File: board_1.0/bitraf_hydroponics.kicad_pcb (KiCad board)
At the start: 2 copper layers, 100 x 50 mm, 44 parts, among them P1 12V, P10 I2C_4, P11 BUZZ, P12 LDR, P13 TEMP_HUM, P14 PROGRAMMER, P15 SPI, P16 RADIO_433, P2 SWITCH_1, P3 SWITCH_2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

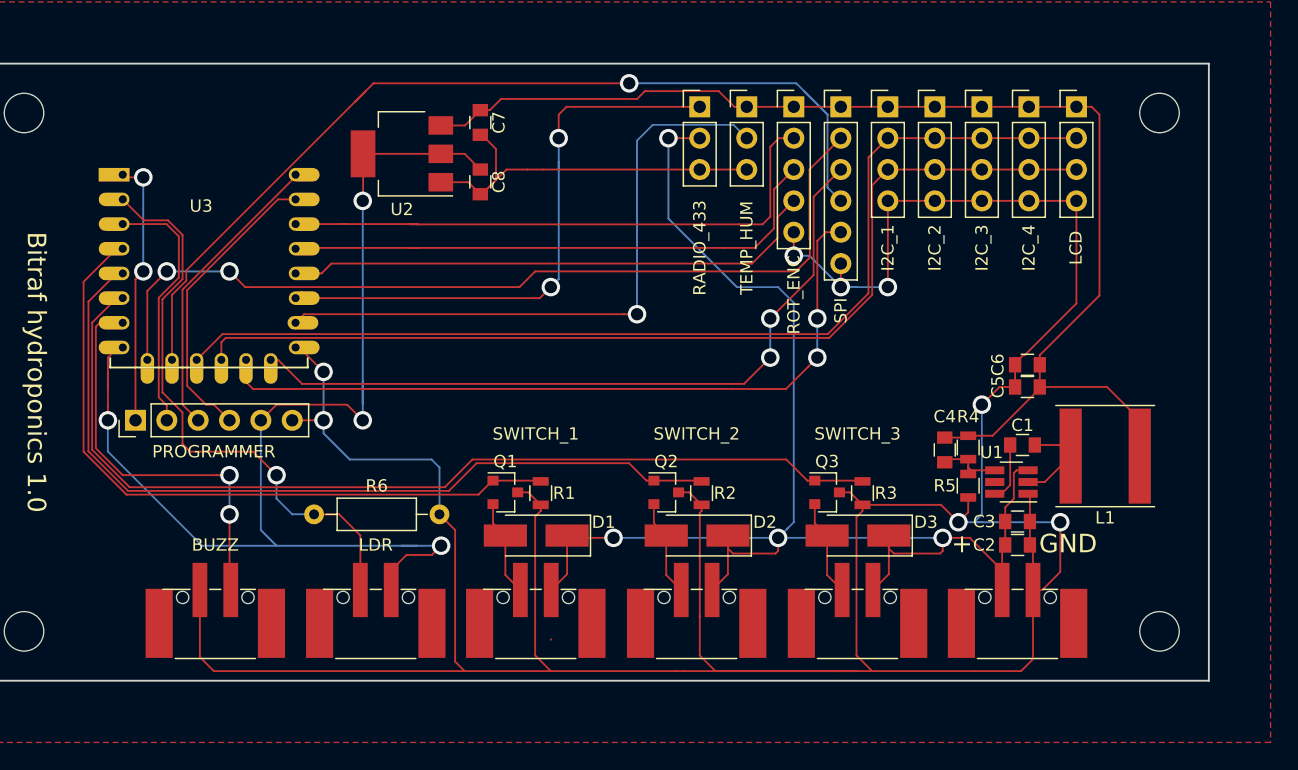
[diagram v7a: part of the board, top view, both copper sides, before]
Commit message: o Switching to new footprints for connectors. Moves everything around a little bit. o Adding some silk screen text to better indicate what goes where.
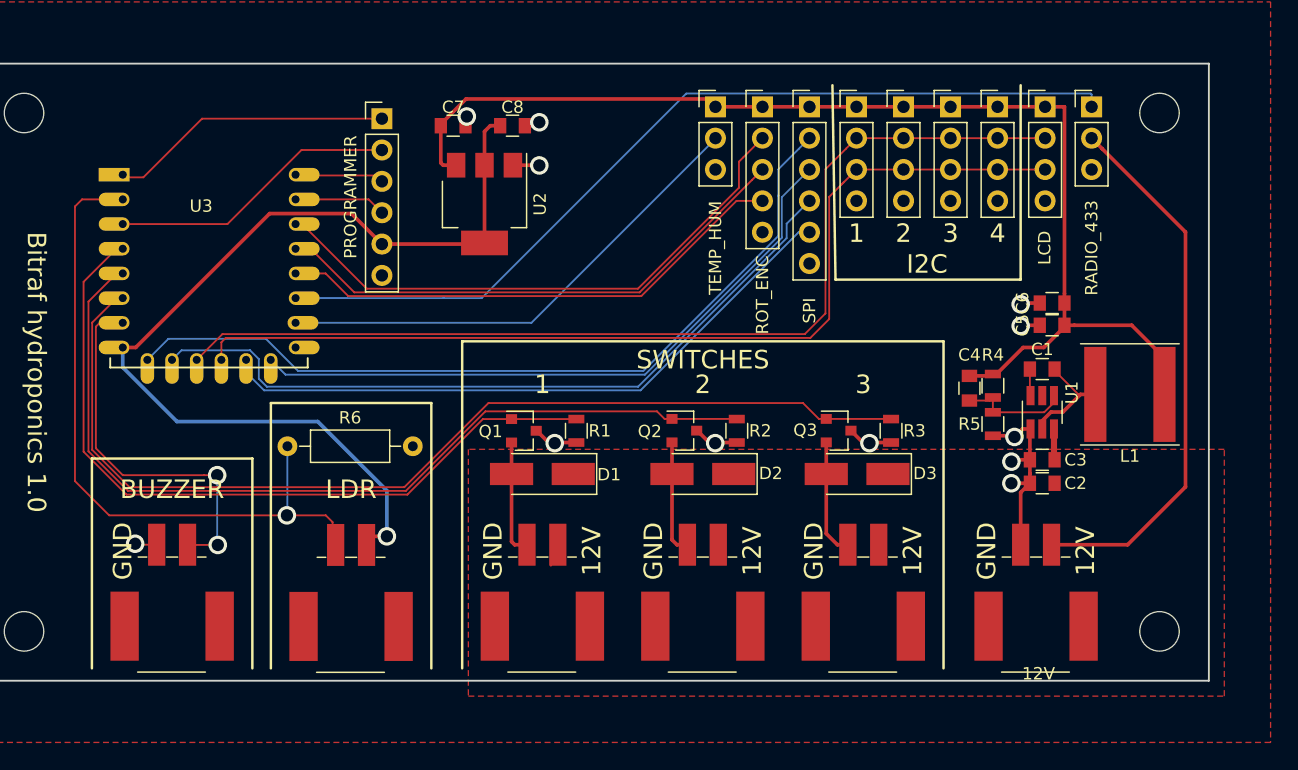
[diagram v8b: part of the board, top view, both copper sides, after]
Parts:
- P1, P12, P2, P3, P4: footprint Connectors_Phoenix:PhoenixContact_PTSM0,5_4-HV-2,5_SMD -> Bitraf:PhoenixContact_PTSM0,5_2-2,5-H_SMD
- P11: value BUZZ -> BUZZER; footprint Connectors_Phoenix:PhoenixContact_PTSM0,5_4-HV-2,5_SMD -> Bitraf:PhoenixContact_PTSM0,5_2-2,5-H_SMD
- moved P16 31.8 mm to (190.5, 63.5)
- moved P14 31.6 mm to (133.0, 64.5), turned to 0 degrees
- moved U2 7.83 mm to (141.3, 71.4), turned to 270 degrees
- moved C1 6.35 mm to (186.5, 84.8)
- moved U1 6.18 mm to (186.5, 88.2), turned to 90 degrees
- moved R6 5.93 mm to (125.3, 91.0)
- moved R1 5.82 mm to (148.8, 89.8)
- moved R2 5.80 mm to (161.8, 89.8)
- moved R3 5.56 mm to (174.2, 89.8)
- moved C2 5.39 mm to (186.5, 94.0), turned to 180 degrees
- moved C3 5.39 mm to (186.5, 92.1), turned to 180 degrees
- moved C4 5.39 mm to (180.6, 86.3)
- moved C5 5.39 mm to (187.3, 81.2)
- moved C6 5.39 mm to (187.3, 79.4)
- moved L1 5.39 mm to (193.6, 86.8)
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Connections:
- P1 pad 1: GND -> +12V
- P1 pad 2: +12V -> GND
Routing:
- net GND: track 314.2 -> 36.4 mm, vias 8 -> 12
- net +12V: track 123.7 -> 47.8 mm, vias 4 -> 0
- net +3V3: track 103.1 -> 78.4 mm, vias 4 -> 1
- net /RF_DATA: track 48.3 -> 72.4 mm, vias 2 -> 0
- net /SPI_MOSI: track 78.4 -> 61.0 mm, vias 1 -> 0
- net /TX: track 24.2 -> 7.22 mm
- net /RX: track 24.2 -> 7.45 mm
- net /TEMP_HUM: track 51.9 -> 40.2 mm, vias 1 -> 0
- net /LDR: track 47.3 -> 56.7 mm
- net /SPI_SCL: track 59.8 -> 53.0 mm, vias 2 -> 0
- net /SPI_MISO: track 60.9 -> 54.4 mm, vias 2 -> 0
- net /SPI_CS: track 72.2 -> 66.5 mm, vias 2 -> 0
- net +5V: track 101.0 -> 95.4 mm
- net /SWITCH_1: track 57.0 -> 61.9 mm
- net /SWITCH_2: track 68.4 -> 72.6 mm
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- added copper zone on F.Cu, net +12V
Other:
- net class Power added: clearance 0.15, trace_width 0.3, via_dia 1.5, via_drill 1
- board text added: "1"
- board text added: "12V"
- board text added: "2"
- board text added: "3"
- board text added: "4"
- board text added: "I2C"
- board text added: "SWITCHES"
- board text removed: "+"
